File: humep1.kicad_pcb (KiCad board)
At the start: 2 copper layers, 50 x 25.2 mm, 8 parts, among them U1 LM1117DT-3.3

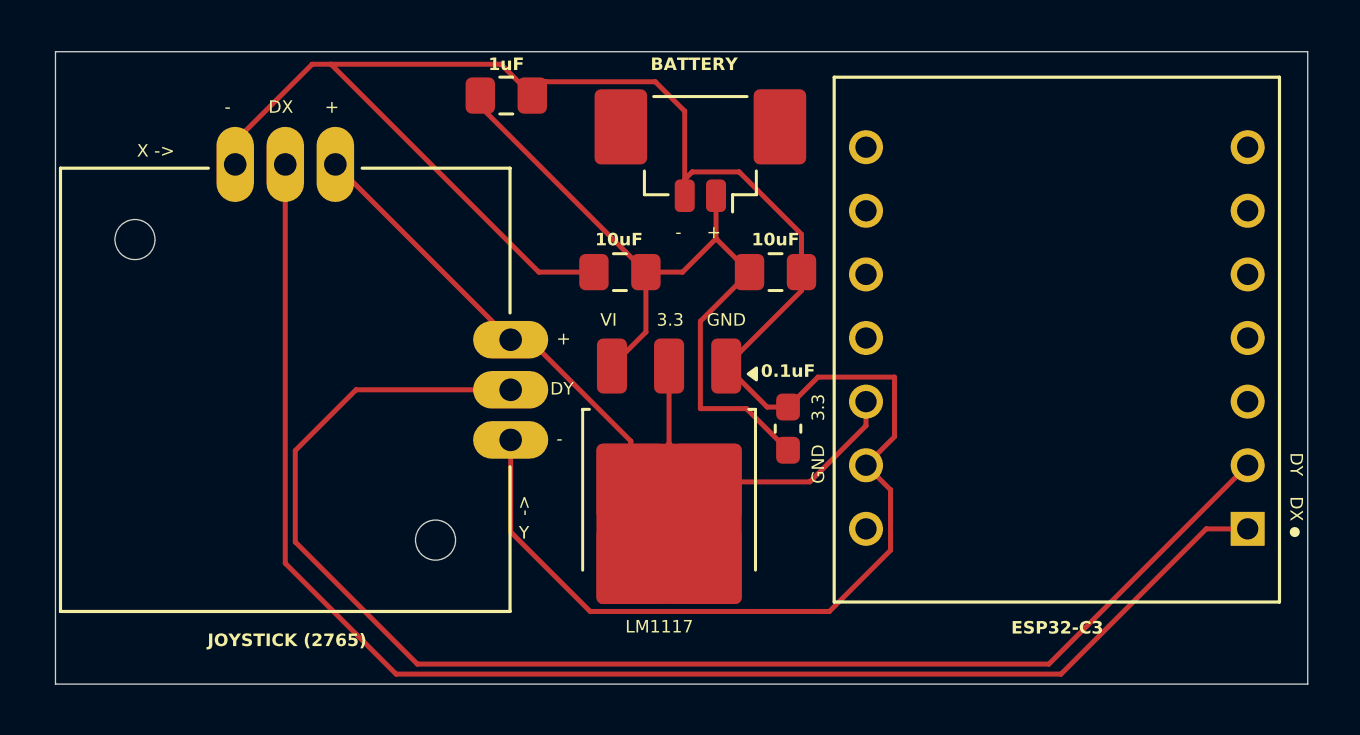
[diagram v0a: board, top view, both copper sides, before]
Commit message: added stiffener, coverlays and exported
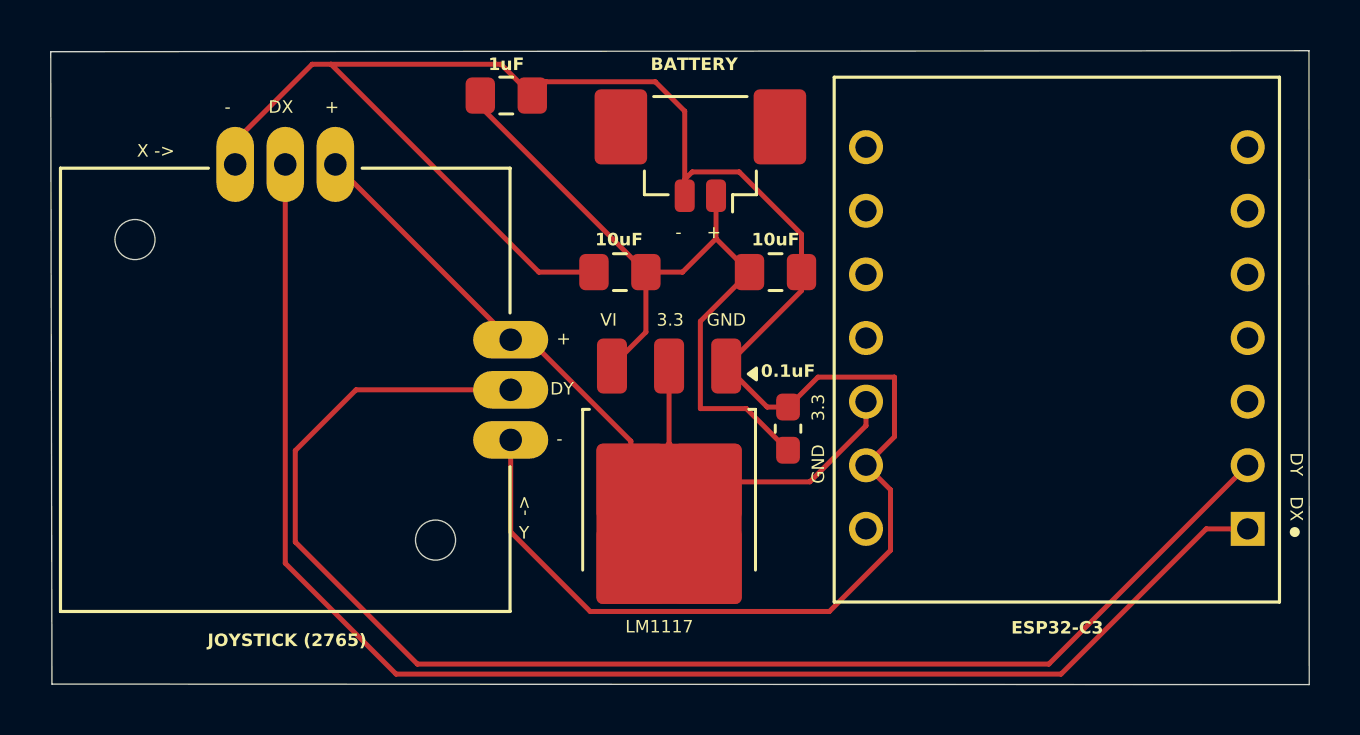
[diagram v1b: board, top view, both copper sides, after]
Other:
- board size 50 x 25.2 mm -> 50.2 x 25.3 mm
